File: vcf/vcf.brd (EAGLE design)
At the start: 85.1 x 107.6 mm, 74 parts, among them IC1 OPA4130U, IC2 OPA4130U, IC3 OPA4130U, IC4 OPA4130U, IC5 OPA4130U, Q1 BC847ASMD, Q2 BC847ASMD, Q3 BC847ASMD, Q4 BC847ASMD, Q5 BC847ASMD, Q6 BC847ASMD, X1 2516-

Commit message: made changes to the vcf board
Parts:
- moved R36 4.02 mm to (35.6, 77.5)
- moved R38 1.80 mm to (47.0, 67.3), turned to 90 degrees
- moved R18 1.27 mm to (55.9, 15.2)
- moved BP 1.27 mm to (73.7, 24.1)
- moved MIN 1.27 mm to (14.0, 24.1)
- moved MIN2 1.27 mm to (43.2, 24.1)
- moved R37 1.27 mm to (41.9, 67.3)
- moved R39 1.27 mm to (39.4, 67.3)
- turned R29 to 270 degrees
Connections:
- removed net N$57: BP.P$1, BP.P$2, BP.P$4
- net GND: now also BP.P$1, BP.P$2, BP.P$4, R6.1
- net N$35: now also IC2.7
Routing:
- net -12V: track 2.54 -> 164.8 mm, vias 0 -> 12
- net +12V: track 82.2 -> 214.8 mm, vias 6 -> 16
- net N$60: track 0.00 -> 107.7 mm, vias 0 -> 4
- net N$2: track 27.2 -> 128.7 mm, vias 4 -> 9
- net N$15: track 36.3 -> 115.1 mm, vias 4 -> 8
- net N$7: track 21.6 -> 86.3 mm, vias 3 -> 6
- net N$29: track 0.00 -> 62.8 mm, vias 0 -> 2
- net N$3: track 10.3 -> 71.5 mm, vias 0 -> 4
- net N$40: track 0.00 -> 58.2 mm, vias 0 -> 4
- net N$6: track 14.1 -> 66.4 mm, vias 2 -> 5
- net N$4: track 3.13 -> 52.5 mm, vias 0 -> 4
- net N$27: track 7.98 -> 56.2 mm, vias 0 -> 4
- net N$51: track 2.54 -> 47.3 mm, vias 0 -> 4
- net N$53: track 0.00 -> 43.7 mm, vias 0 -> 4
- net N$41: track 0.00 -> 39.8 mm, vias 0 -> 4
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- added copper zone on layer 16, net GND

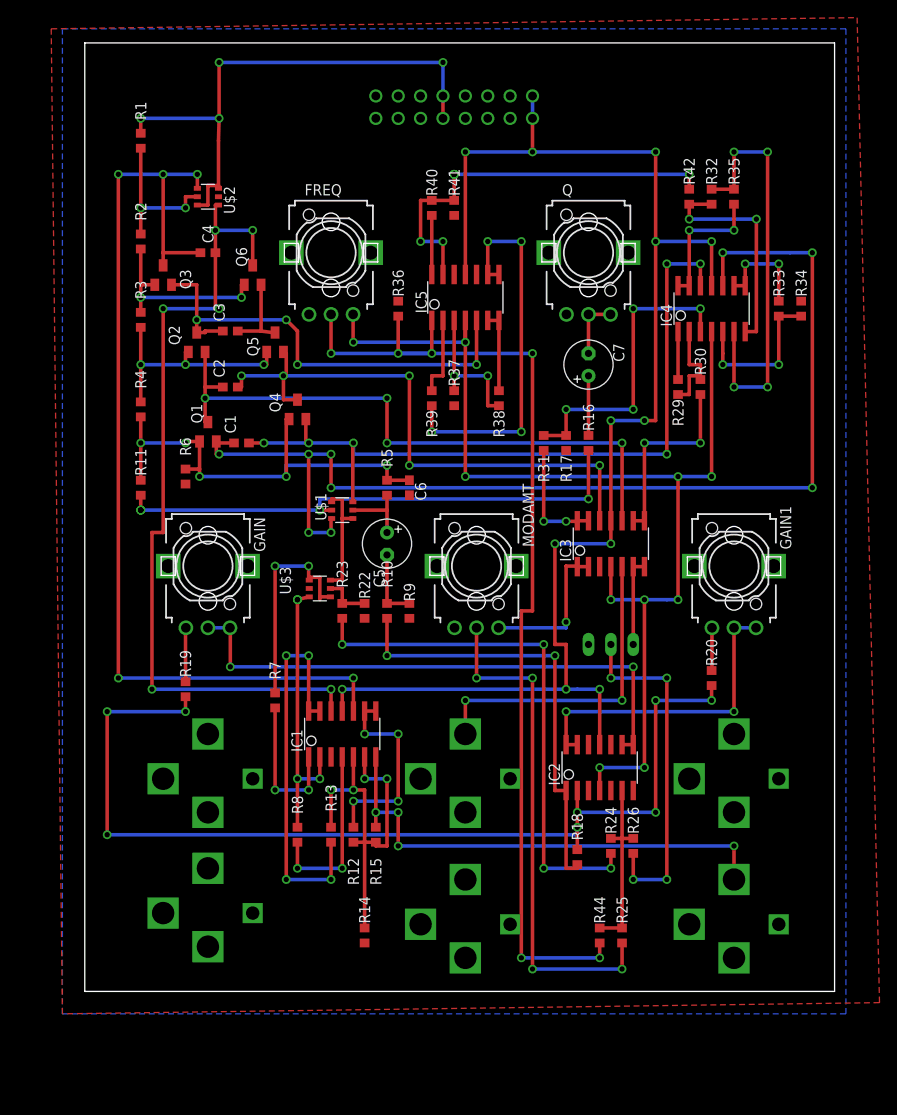
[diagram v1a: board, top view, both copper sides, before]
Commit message: changed layouts, changed vias to round.
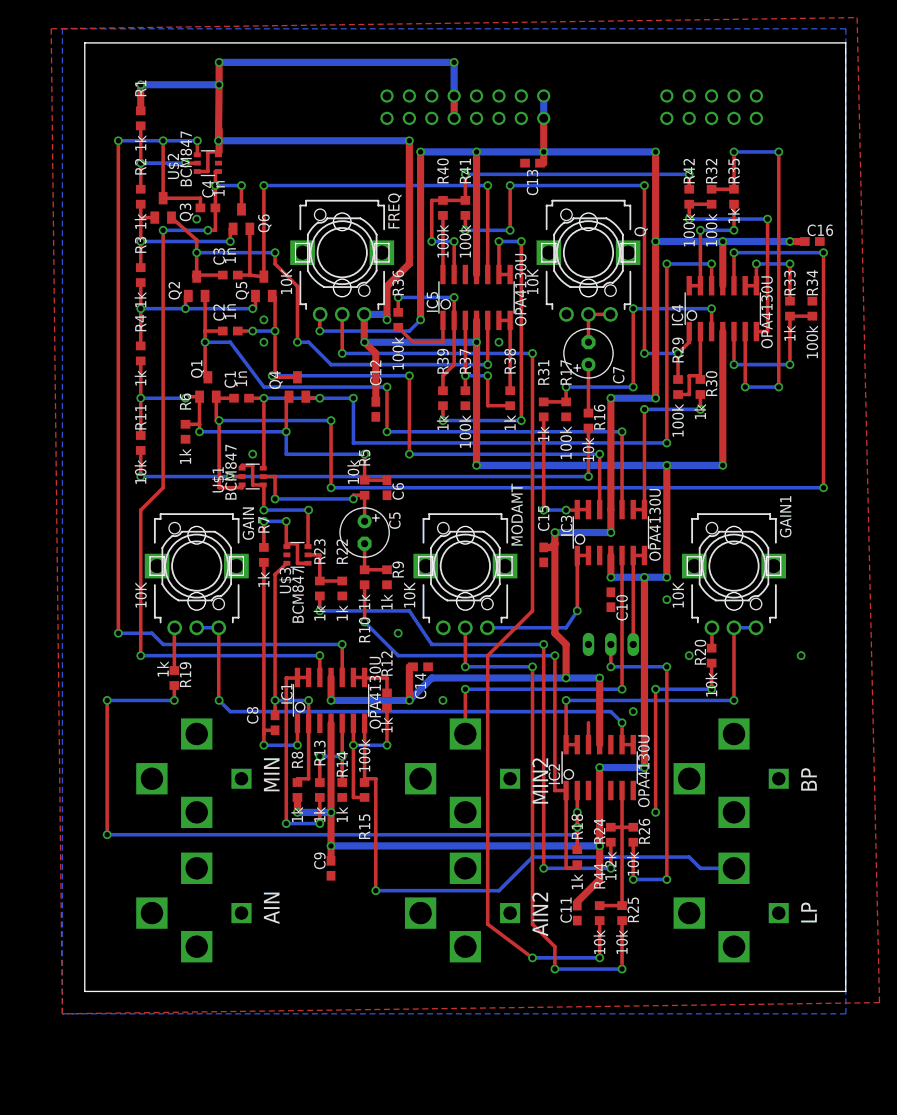
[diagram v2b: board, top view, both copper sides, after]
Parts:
- removed X1: 2516-, dan:PAK100/2500-16
- added C10, C11, C12, C13, C14, C15, C16, C9: 1u, dan:C0603
- added C8: 100p, dan:C0603
- added POWER: 2516-, dan:PAK100/2500-16
- added XPAND: 2510-, dan:PAK100/2500-10
- C5: value (none) -> .47u
- C6: value (none) -> 1u
- C7: value (none) -> 100n
- moved R14 16.7 mm to (29.2, 22.9)
- moved R7 16.6 mm to (20.3, 49.5)
- moved R12 15.7 mm to (34.3, 33.0)
- moved U$1 10.9 mm to (19.1, 58.4)
- moved Q3 7.62 mm to (8.89, 88.9)
- moved Q5 6.48 mm to (20.3, 80.0)
- moved Q6 6.48 mm to (17.8, 87.6)
- moved C2 6.35 mm to (16.5, 74.9)
- moved Q2 6.35 mm to (12.7, 80.0)
- moved C3 6.35 mm to (16.5, 81.3)
- moved R4 6.35 mm to (6.35, 72.4)
- moved R15 5.24 mm to (31.8, 22.9)
- moved R13 5.24 mm to (26.7, 22.9)
- moved C4 5.08 mm to (14.0, 88.9)
- moved C1 5.08 mm to (17.8, 67.3)
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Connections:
- net +12V: now also C10.1, C11.1, C12.1, C9.1, POWER.10, POWER.9; no longer X1.10, X1.9
- net -12V: now also C13.1, C14.1, C15.1, C16.1, POWER.1, POWER.2; no longer X1.1, X1.2
- net GND: now also C10.2, C11.2, C12.2, C13.2, C14.2, C15.2, C16.2, C9.2, POWER.3, POWER.4, POWER.5, POWER.6, POWER.7, POWER.8, XPAND.1, XPAND.2, XPAND.3, XPAND.5, XPAND.7, XPAND.9; no longer X1.3, X1.4, X1.5, X1.6, X1.7, X1.8
- net N$17: now also C8.2
- net N$19: now also C8.1
- net N$27: now also XPAND.10
- net N$47: now also XPAND.6
- net N$52: now also XPAND.4
- net N$58: now also XPAND.8
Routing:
- net +12V: track 214.8 -> 311.7 mm, vias 16 -> 21
- net -12V: track 164.8 -> 222.5 mm, vias 12 -> 17
- net N$47: track 5.44 -> 55.9 mm, vias 0 -> 6
- net N$5: track 9.49 -> 54.0 mm, vias 0 -> 2
- net N$24: track 44.8 -> 25.9 mm, vias 4 -> 2
- net N$23: track 23.3 -> 5.56 mm, vias 4 -> 0
- net N$26: track 27.4 -> 12.2 mm
- net N$16: track 24.8 -> 13.4 mm
- net N$17: track 16.9 -> 28.3 mm
- net N$56: track 9.25 -> 19.1 mm, vias 0 -> 2
- net N$14: track 8.11 -> 17.4 mm, vias 0 -> 2
- net N$27: track 56.2 -> 63.8 mm, vias 4 -> 1
- net N$4: track 52.5 -> 59.5 mm
- net N$15: track 115.1 -> 108.7 mm
- net N$53: track 43.7 -> 38.5 mm
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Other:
- board size 85.1 x 107.6 mm -> 86.3 x 107.6 mm
- board text added: "AIN"
- board text added: "AIN2"
- board text added: "BP"
- board text added: "LP"
- board text added: "MIN"
- board text added: "MIN2"

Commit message: changed a bunch of stuff.
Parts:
- added C17, C18, C19, C20: 1u, dan:C0603
- C5: value .47u -> 4.7u
- C7: value 100n -> 4.7u
- R14, R7: value 1k -> 10k
- R15, R17, R29, R32, R34, R36, R37: value 100k -> 10k
- R20: value 10k -> 1k
- R8: value 1k -> 2Meg
- moved C13 69.2 mm to (59.7, 25.4), turned to 90 degrees
- moved R44 67.6 mm to (29.2, 69.8), turned to 270 degrees
- moved R13 59.3 mm to (69.8, 63.5)
- moved R14 59.3 mm to (72.4, 63.5)
- moved R15 55.9 mm to (74.9, 58.4)
- moved R36 50.0 mm to (81.3, 55.9)
- moved R18 49.1 mm to (38.1, 61.0), turned to 90 degrees
- moved C8 48.6 mm to (38.1, 76.2)
- moved R24 47.1 mm to (48.3, 63.5), turned to 90 degrees
- moved R26 47.1 mm to (50.8, 63.5), turned to 270 degrees
- moved C12 46.4 mm to (78.7, 58.4)
- moved R12 45.8 mm to (72.4, 58.4)
- moved R39 44.7 mm to (83.8, 55.9)
- moved C15 38.6 mm to (78.7, 77.5), turned to 90 degrees
- moved R20 38.1 mm to (38.1, 57.1), turned to 90 degrees
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- renumbered MIN2 to VPEROCT
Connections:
- removed net N$49: IC4.8, IC4.9, R33.2
- new net N$57: GAIN.2, R19.1
- new net N$63: GAIN.3, IC1.1, IC1.2
- net +12V: now also C17.1, C19.1
- net -12V: now also C18.1, C20.1
- net GND: now also C17.2, C18.2, C19.2, C20.2, GAIN.1, GAIN1.1, IC5.10, IC5.3, Q.3; no longer IC1.3, IC2.3, IC2.5
- net N$15: now also IC5.2; no longer IC2.2
- net N$17: now also IC5.14; no longer IC1.1
- net N$18: now also IC1.3; no longer IC2.10
- net N$19: now also IC5.13; no longer IC1.2
- net N$2: now also IC3.10; no longer IC4.10
- net N$20: now also IC5.1; no longer IC2.1
- net N$23: now also IC2.1, IC2.2, R13.1; no longer IC1.8, IC1.9, R12.1
- net N$24: now also IC5.5, R44.2; no longer IC1.13, IC1.14, R13.1
- net N$25: now also IC4.2; no longer IC1.6
- net N$26: now also IC4.3; no longer IC1.5
- net N$27: now also IC4.1; no longer IC1.7
- net N$28: now also IC2.8, IC2.9, R38.2; no longer GAIN.1, R19.1
- net N$29: now also IC1.8, IC1.9, MODAMT.3; no longer GAIN.2, GAIN.3, IC2.8, IC2.9
- net N$3: now also IC3.5; no longer IC3.10
- net N$30: now also IC1.6, IC1.7; no longer GAIN1.2, IC2.13, IC2.14
- net N$32: no longer Q.3
- net N$33: now also IC1.5; no longer IC2.12
- net N$35: now also IC2.6, R12.1; no longer R23.1, R24.2
- net N$36: now also IC5.6; no longer IC2.6, R44.2
- net N$37: now also R31.2; no longer MODAMT.3
- net N$38: now also IC1.13, IC1.14; no longer IC3.6, IC3.7
- net N$39: now also IC3.8, IC3.9, R33.2; no longer IC3.13, IC3.14, R31.2
- net N$4: now also IC2.10; no longer IC5.5
- net N$42: now also IC2.13, IC2.14, R39.2; no longer IC3.3, MIN.P$3
- net N$43: now also IC1.12; no longer IC3.5
- net N$44: now also IC3.6, IC3.7; no longer IC3.8, IC3.9
- net N$45: now also IC4.10; no longer IC4.3
- net N$46: now also IC4.9; no longer IC4.2
- net N$47: now also IC4.8; no longer IC4.1
- net N$48: now also IC3.13, IC3.14; no longer IC4.13, IC4.14
- net N$5: now also IC2.12; no longer IC5.10
- net N$50: now also IC1.10, MIN.P$3; no longer IC5.6, IC5.7, R38.2
- net N$51: now also IC4.13; no longer IC4.6
- net N$52: now also IC4.14; no longer IC4.7
- net N$53: now also IC5.7, R23.1, R24.2; no longer IC5.8, IC5.9, R39.2
- net N$54: now also IC4.12; no longer IC4.5
- net N$55: now also IC4.5; no longer IC5.3
- net N$56: now also IC4.6; no longer IC5.2
- net N$58: now also IC4.7; no longer IC5.1
- net N$59: now also IC5.9; no longer IC5.13
- net N$6: now also IC3.3; no longer IC3.12
- net N$61: now also IC5.8; no longer IC5.14
- net N$62: now also GAIN1.2; no longer GAIN1.1
- net N$7: now also IC3.12; no longer IC4.12
- net N$8: now also IC2.3; no longer IC1.12
- net N$9: now also IC2.5; no longer IC1.10
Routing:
- net -12V: track 222.5 -> 23.4 mm, vias 17 -> 0
- net +12V: track 311.7 -> 159.0 mm, vias 21 -> 7
- net N$2: track 132.4 -> 21.6 mm, vias 6 -> 4
- net N$60: track 111.1 -> 6.12 mm, vias 4 -> 0
- net N$15: track 108.7 -> 8.82 mm, vias 8 -> 0
- net N$42: track 0.00 -> 99.4 mm, vias 0 -> 4
- net N$9: track 108.0 -> 26.4 mm, vias 5 -> 4
- net N$18: track 0.00 -> 80.0 mm, vias 0 -> 3
- net N$8: track 90.7 -> 15.2 mm, vias 6 -> 2
- net N$7: track 90.2 -> 16.5 mm, vias 6 -> 2
- net N$23: track 5.56 -> 74.1 mm, vias 0 -> 4
- net N$63: track 0.00 -> 66.0 mm, vias 0 -> 4
- net N$19: track 32.2 -> 98.2 mm, vias 2 -> 6
- net N$3: track 75.3 -> 14.8 mm, vias 4 -> 2
- net N$40: track 60.5 -> 3.58 mm, vias 4 -> 0
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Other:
- board text added: "VOCT"
- board text removed: "MIN2"

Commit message: almost done with the filter board
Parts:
- moved R42 16.9 mm to (71.1, 72.4), turned to 270 degrees
- moved R32 15.3 mm to (76.2, 74.9), turned to 90 degrees
- moved C15 8.98 mm to (80.0, 86.4)
- moved R34 8.98 mm to (85.1, 86.4)
- moved R33 8.98 mm to (82.5, 86.4)
- moved R17 7.62 mm to (62.2, 72.4)
- moved R31 7.62 mm to (64.8, 72.4)
- moved R35 6.84 mm to (67.3, 82.5), turned to 90 degrees
- moved IC3 6.48 mm to (73.7, 85.1)
- moved C19 6.48 mm to (73.7, 77.5)
- moved R10 5.39 mm to (35.6, 45.7)
- moved C10 5.24 mm to (26.7, 27.9)
- moved C18 5.24 mm to (45.7, 92.7), turned to 270 degrees
- moved C14 4.02 mm to (26.7, 49.5)
- moved C16 4.02 mm to (73.7, 92.7)
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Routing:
- net -12V: track 23.4 -> 224.0 mm, vias 0 -> 14
- net +12V: track 159.0 -> 322.7 mm, vias 7 -> 23
- net N$8: track 15.2 -> 121.8 mm, vias 2 -> 7
- net N$27: track 53.1 -> 153.2 mm, vias 3 -> 9
- net N$9: track 26.4 -> 122.5 mm, vias 4 -> 7
- net N$2: track 21.6 -> 115.9 mm, vias 4 -> 6
- net N$3: track 14.8 -> 98.5 mm, vias 2 -> 6
- net N$7: track 16.5 -> 99.4 mm, vias 2 -> 4
- net N$47: track 23.7 -> 98.3 mm, vias 2 -> 6
- net N$6: track 16.3 -> 88.3 mm, vias 2 -> 8
- net N$61: track 2.90 -> 70.8 mm, vias 0 -> 4
- net N$62: track 0.00 -> 67.7 mm, vias 0 -> 6
- net N$58: track 11.8 -> 75.4 mm, vias 0 -> 4
- net N$4: track 15.1 -> 73.4 mm, vias 2 -> 6
- net N$15: track 8.82 -> 62.5 mm, vias 0 -> 4
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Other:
- board size 86.3 x 107.6 mm -> 88.9 x 107.6 mm

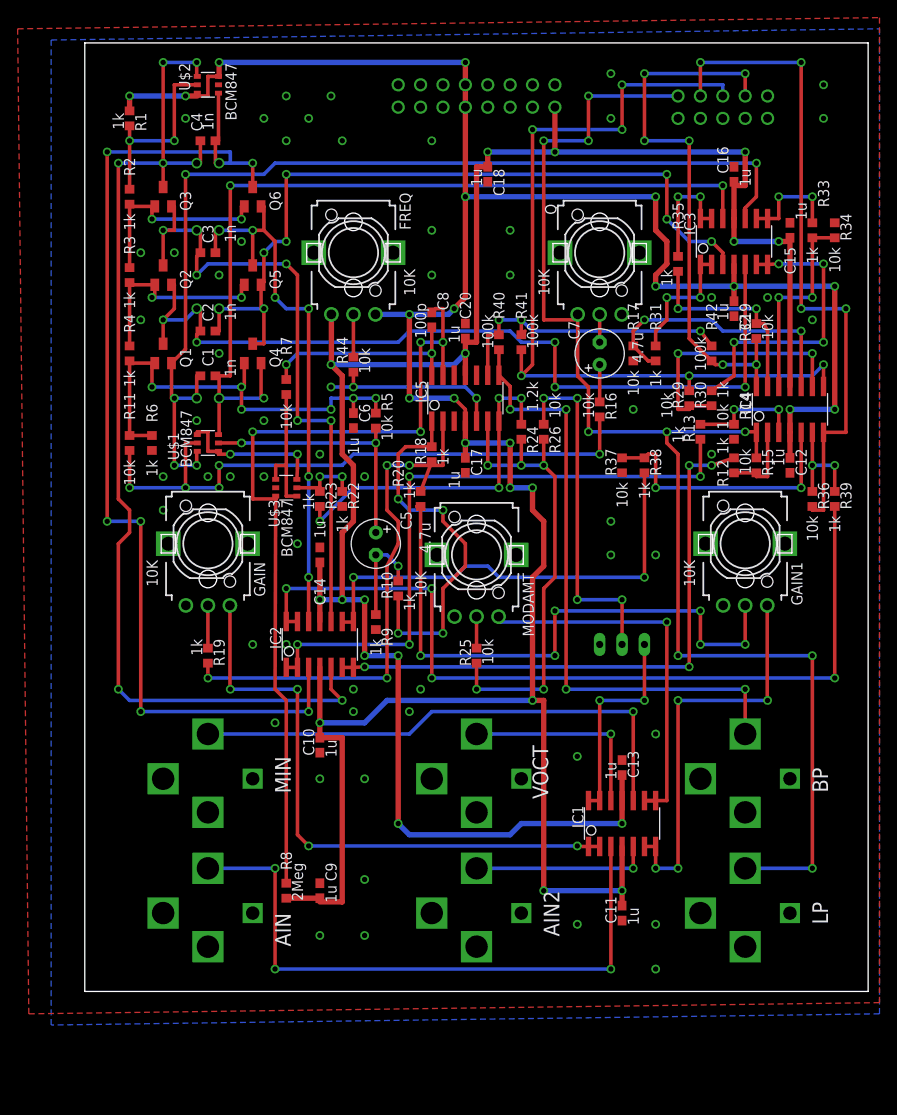
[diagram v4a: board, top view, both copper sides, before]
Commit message: vcf, added protection and input resistors.  Added holes on corners.  fixed silkscreen.  generated viable gerbers for vcf.
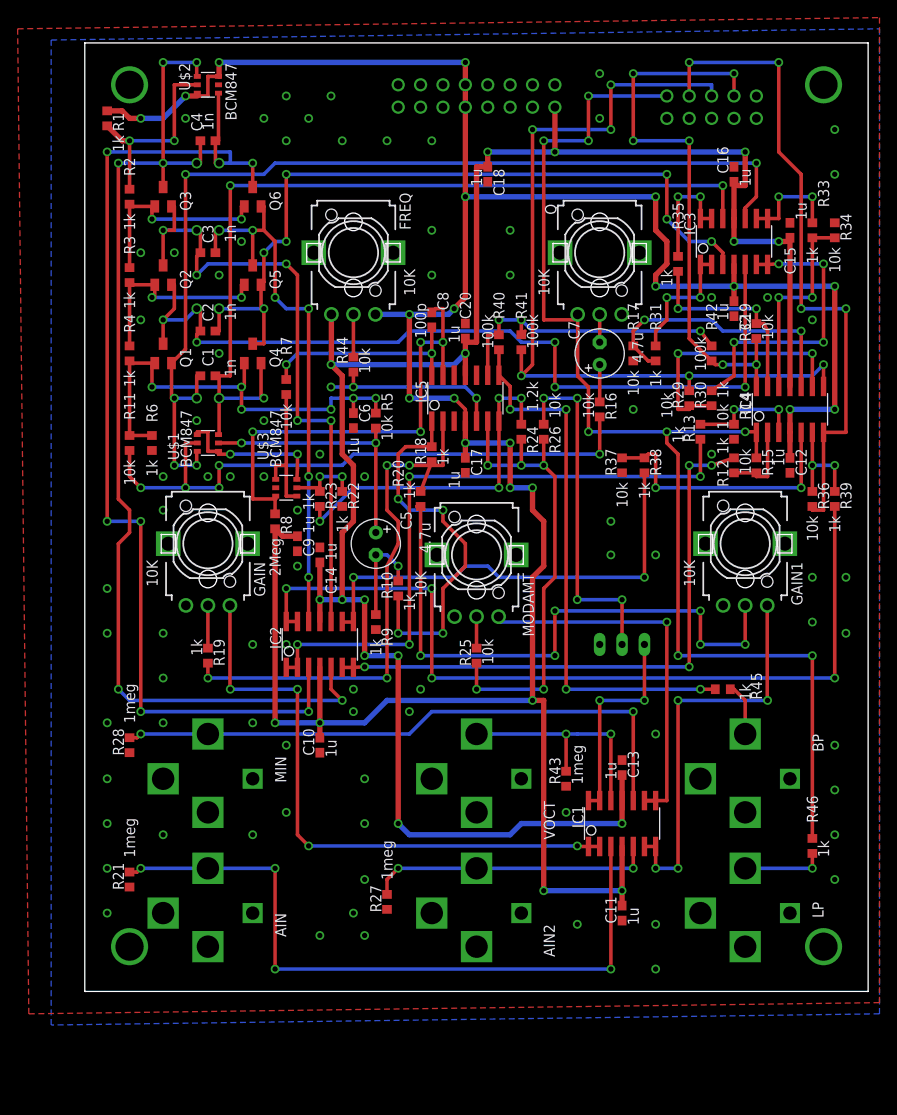
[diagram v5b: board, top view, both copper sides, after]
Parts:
- added R21, R27, R28, R43: 1meg, dan:R0603
- added R45, R46: 1k, dan:R0603
- moved R8 41.9 mm to (21.6, 53.3)
- moved C9 39.5 mm to (24.1, 50.8), turned to 270 degrees
- moved R1 2.54 mm to (2.54, 99.1)
- moved XPAND 1.27 mm to (71.1, 100.3)
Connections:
- new net N$49: BP.P$3, R45.1
- new net N$64: LP.P$3, R46.1
- net GND: now also R21.1, R27.1, R28.1, R43.1
- net N$18: now also R21.2
- net N$27: now also R46.2; no longer LP.P$3
- net N$33: now also R27.2
- net N$43: now also R43.2
- net N$50: now also R28.2
- net N$61: now also R45.2; no longer BP.P$3
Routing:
- net N$19: track 95.7 -> 53.3 mm
- net N$33: track 20.3 -> 32.6 mm, vias 1 -> 2
- net N$27: track 153.2 -> 140.9 mm, vias 9 -> 8
- net N$64: track 0.00 -> 9.31 mm, vias 0 -> 1
- net N$50: track 59.4 -> 68.5 mm, vias 1 -> 2
- net N$18: track 71.1 -> 80.1 mm, vias 3 -> 4
- net N$61: track 70.8 -> 62.3 mm
- net N$49: track 0.00 -> 6.03 mm
- net +12V: track 322.7 -> 327.0 mm, vias 23 -> 24
- net N$43: track 22.8 -> 27.0 mm, vias 1 -> 2
- net N$10: track 21.2 -> 22.8 mm
- net N$52: track 63.4 -> 64.7 mm
- net N$47: track 98.3 -> 97.1 mm
- net N$22: track 71.3 -> 70.5 mm

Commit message: added some critical stuff.  sent the board to pcbway for checking.
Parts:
- added R47, R48: 1k, dan:R0603
- moved R35 5.08 mm to (67.3, 87.6)
- moved FREQ 2.54 mm to (27.9, 83.8)
- moved MODAMT 2.54 mm to (44.5, 52.1)
- moved Q 2.54 mm to (61.0, 83.8)
- moved R31 1.27 mm to (66.0, 72.4)
- moved GAIN 1.27 mm to (14.0, 52.1)
- moved GAIN1 1.27 mm to (74.9, 52.1)
- moved R17 1.27 mm to (63.5, 72.4)
- moved C7 1.27 mm to (59.7, 72.4)
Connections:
- new net N$65: FREQ.1, R48.2
- new net N$66: FREQ.3, R47.1
- net +12V: now also R47.2; no longer FREQ.3
- net -12V: now also R48.1; no longer FREQ.1
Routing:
- net N$10: track 22.8 -> 33.0 mm, vias 2 -> 4
- net N$53: track 39.2 -> 44.6 mm
- net N$51: track 22.9 -> 28.0 mm
- net N$48: track 13.1 -> 7.98 mm
- net N$65: track 0.00 -> 4.09 mm
- net N$66: track 0.00 -> 3.26 mm
- net N$55: track 30.6 -> 33.7 mm
- net N$22: track 70.5 -> 67.5 mm
- net N$40: track 3.58 -> 6.12 mm
- net N$28: track 52.3 -> 54.4 mm
- net N$45: track 31.3 -> 29.3 mm
- net N$27: track 140.9 -> 142.5 mm
- net N$5: track 63.0 -> 61.5 mm
- net N$63: track 68.6 -> 69.8 mm
- net N$62: track 67.7 -> 68.9 mm
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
